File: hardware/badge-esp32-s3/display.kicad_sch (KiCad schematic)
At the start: 2 parts

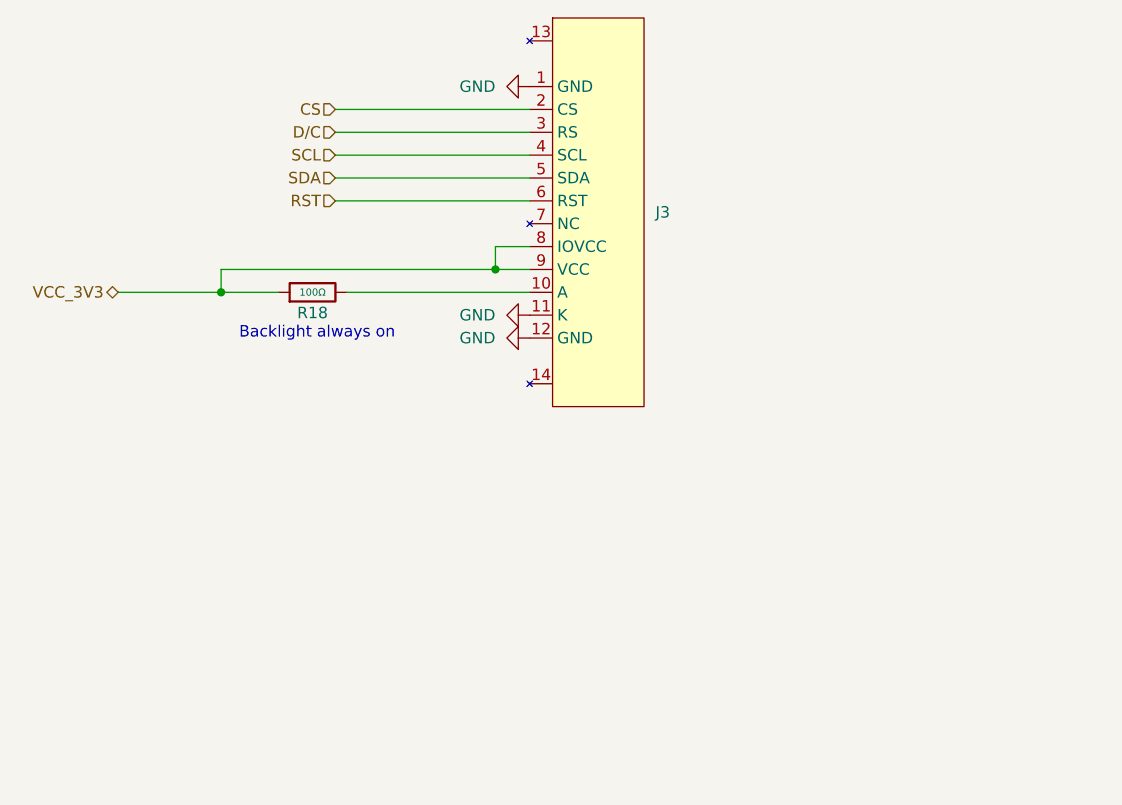
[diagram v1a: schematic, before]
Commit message: Fix LCD connector
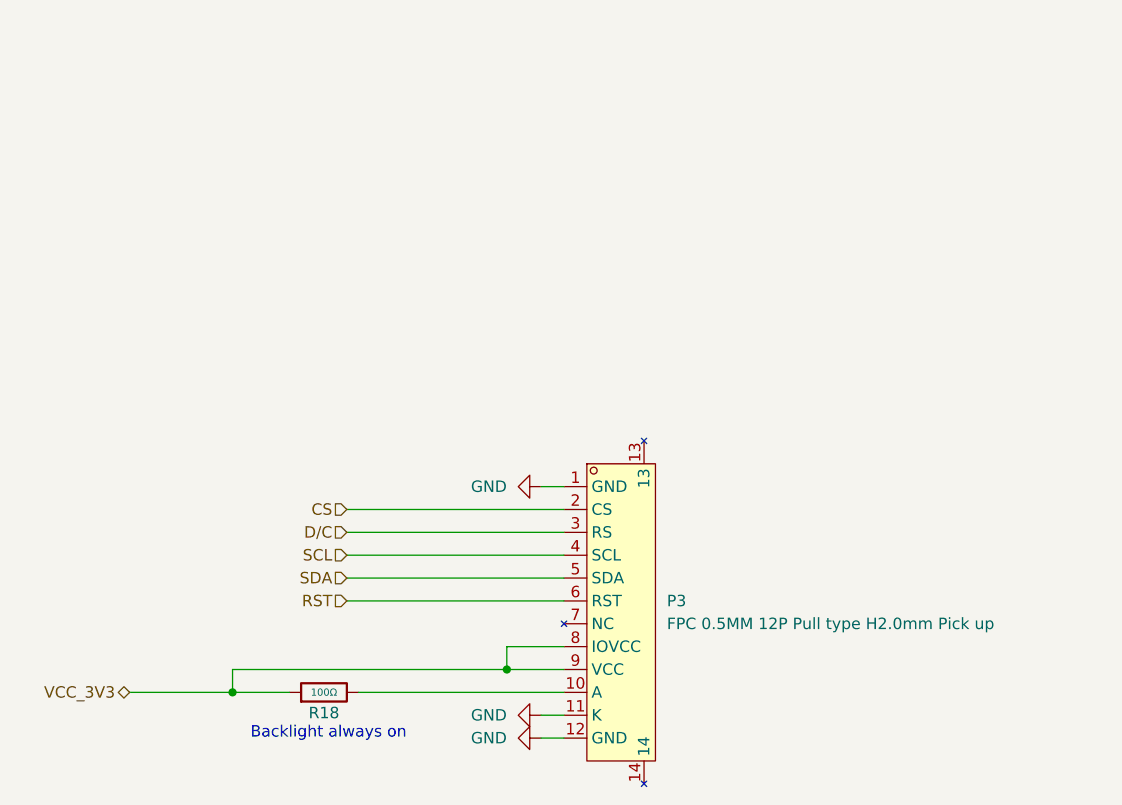
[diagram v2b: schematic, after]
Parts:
- removed J3: ~, lcsc-lib:FPC-SMD_AFC01-S12FCA-00, symbol lcsc-lib:JUSHUO_AFC01-S12FCA-00
- added P3: FPC 0.5MM 12P Pull type H2.0mm Pick up, lcsc-lib:FPC-SMD_12P-L11.5-W5.4-P0.50, symbol lcsc-lib:FPC0.5MM12PPulltypeH2.0mmPickup
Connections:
- net CS: now also P3.2 (CS)
- net D/C: now also P3.3 (RS)
- net GND: now also P3.1 (GND), P3.11 (K), P3.12 (GND)
- net RST: now also P3.6 (RST)
- net SCL: now also P3.4 (SCL)
- net SDA: now also P3.5 (SDA)
- net VCC_3V3: now also P3.8 (IOVCC), P3.9 (VCC)
- net at R18.2: now also P3.10 (A)
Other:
- moved on the sheet: R18
